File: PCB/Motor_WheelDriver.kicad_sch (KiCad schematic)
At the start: 21 parts, among them J7 39501-1002, J8 39501-1002, U1 125700D00000G, U2 125700D00000G

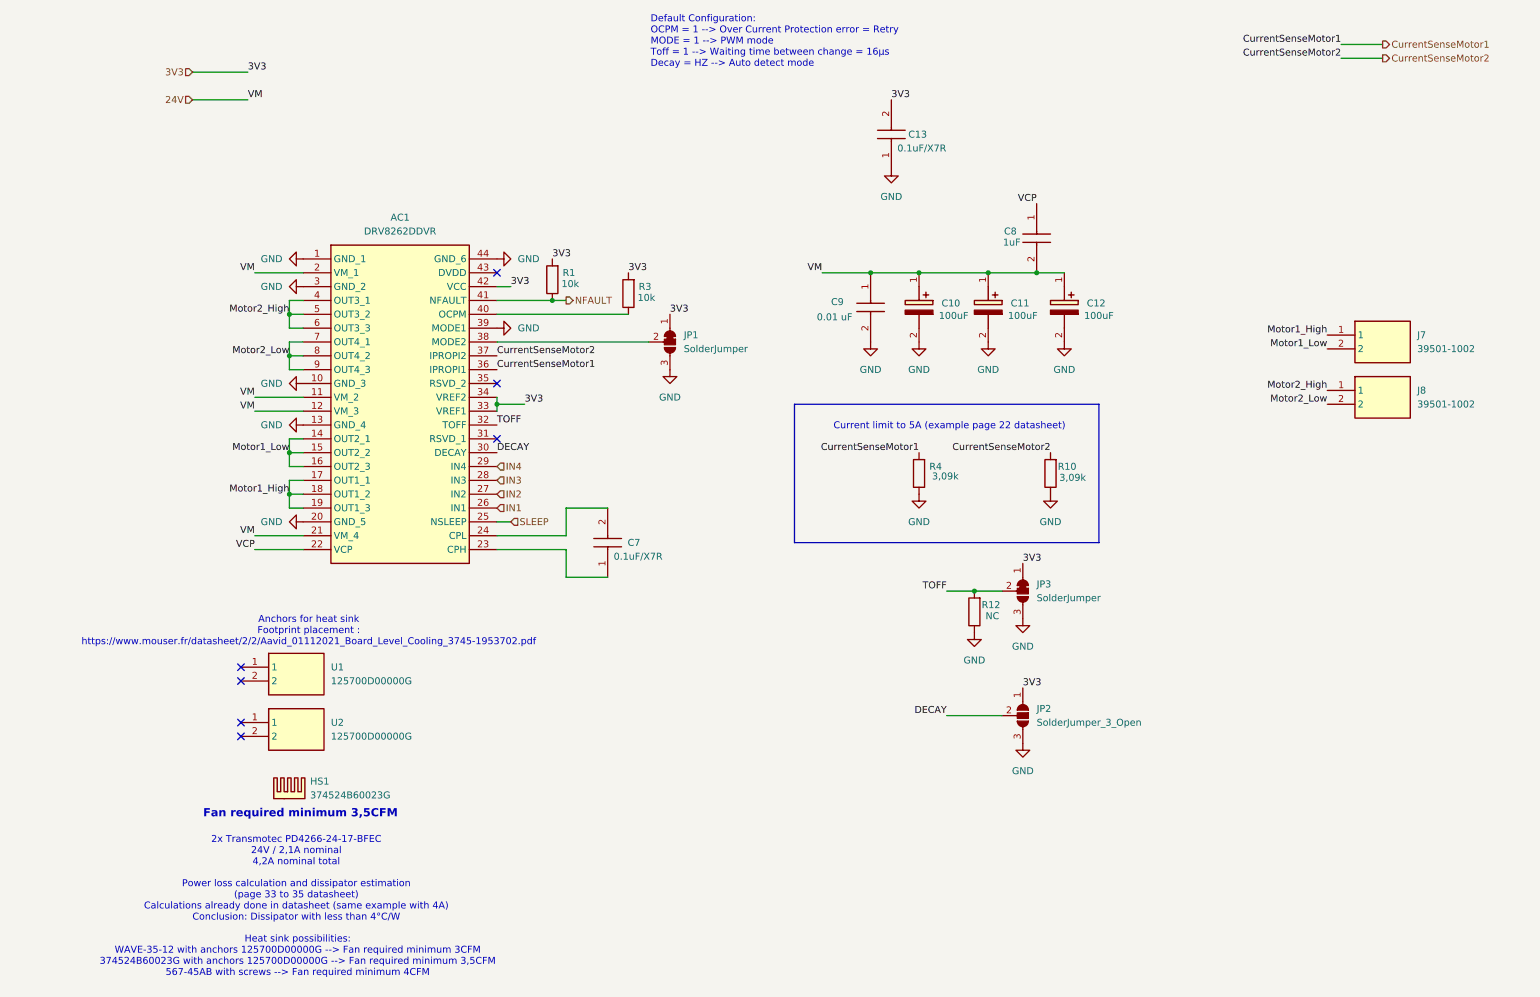
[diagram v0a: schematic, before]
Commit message: Updated a lot of stuff:
Added encoders,
Added 5V power supply for actuators
Added 12V power supply for actuators
Renamed sheets to be clearer
Added usb debug
Modify MCU sheet to be A3 format
Linked some pins
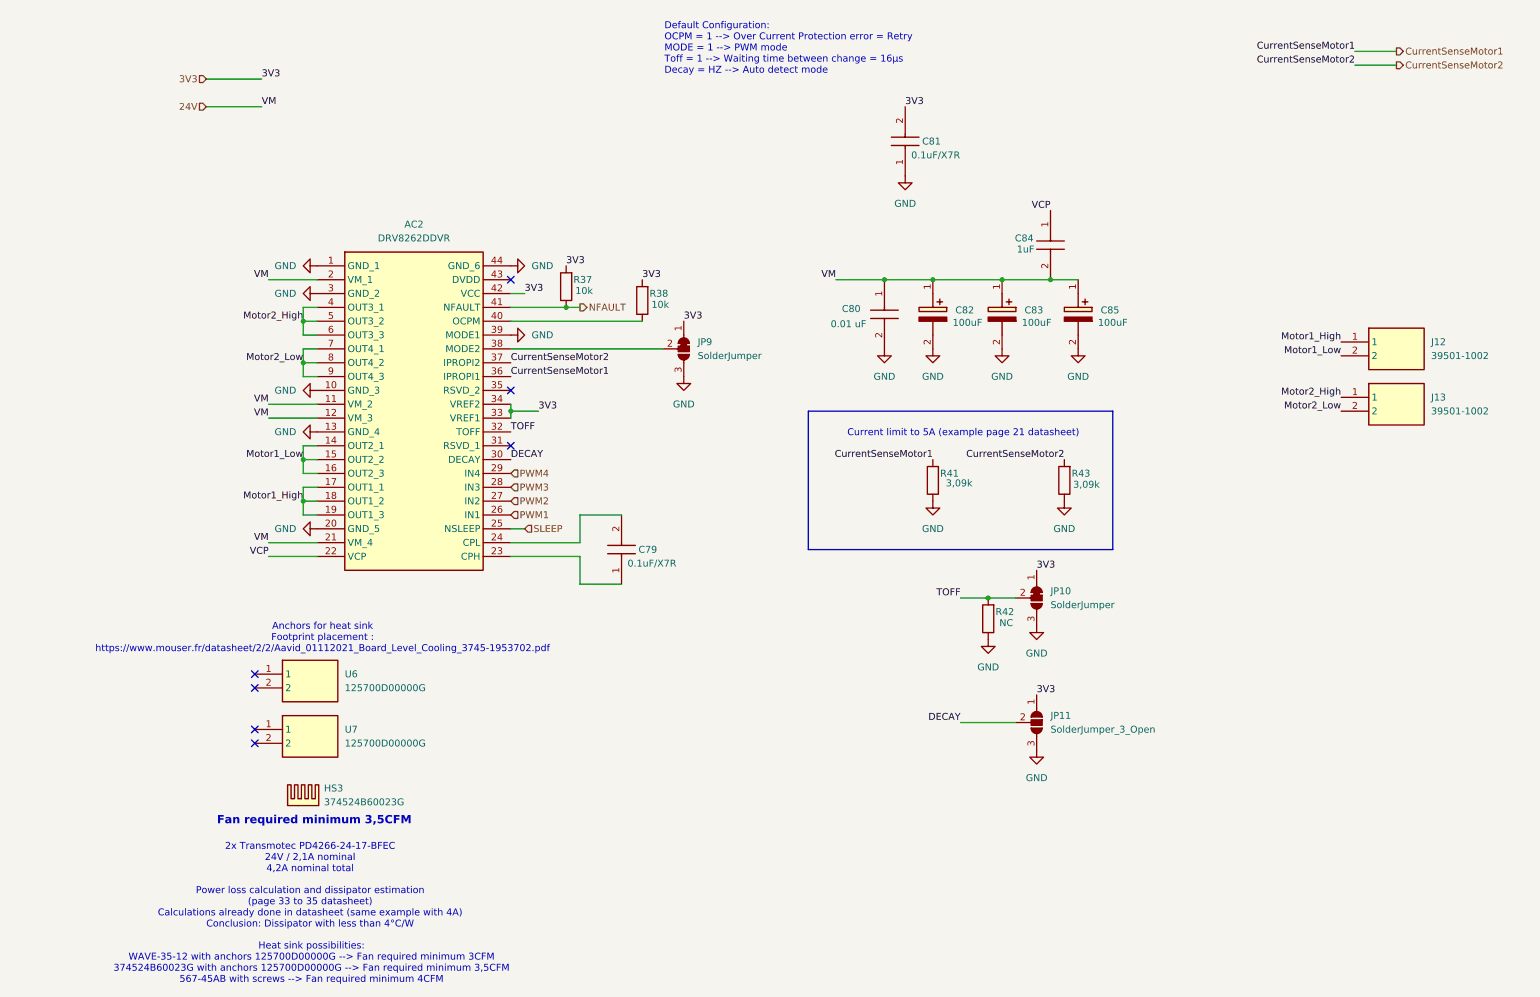
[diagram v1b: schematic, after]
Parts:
- removed AC1: DRV8262DDVR, SOP64P810X120-44N, symbol SamacSys:DRV8262DDVR
- removed C10, C11, C12: 100uF, CAPAE660X800N, symbol SamacSys_Parts:UCH1V101MCS1GS
- removed C13, C7: 0.1uF/X7R, CAPC2012X94N, symbol SamacSys_Parts:0805DC104MAT2A
- removed C8: 1uF, CAPC2012X94N, symbol SamacSys_Parts:0805DC104MAT2A
- removed C9: 0.01 uF, CAPC2012X94N, symbol SamacSys_Parts:0805DC104MAT2A
- removed HS1: 374524B60023G, symbol Mechanical:Heatsink
- removed J7, J8: 39501-1002, 395011002, symbol SamacSys:39501-1002
- removed JP1, JP3: SolderJumper, Jumper:SolderJumper-3_P1.3mm_Bridged12_RoundedPad1.0x1.5mm, symbol Jumper:SolderJumper_3_Bridged12
- removed JP2: SolderJumper_3_Open, symbol Jumper:SolderJumper_3_Open
- removed R1, R3: 10k, symbol Device:R
- removed R10, R4: 3,09k, symbol Device:R
- removed R12: NC, symbol Device:R
- removed U1, U2: 125700D00000G, 125700D00000G, symbol SamacSys_new:125700D00000G
- added AC2: DRV8262DDVR, SOP64P810X120-44N, symbol SamacSys:DRV8262DDVR
- added C79, C81: 0.1uF/X7R, CAPC2012X94N, symbol SamacSys_Parts:0805DC104MAT2A
- added C80: 0.01 uF, CAPC2012X94N, symbol SamacSys_Parts:0805DC104MAT2A
- added C82, C83, C85: 100uF, CAPAE660X800N, symbol SamacSys_Parts:UCH1V101MCS1GS
- added C84: 1uF, CAPC2012X94N, symbol SamacSys_Parts:0805DC104MAT2A
- added HS3: 374524B60023G, symbol Mechanical:Heatsink
- added J12, J13: 39501-1002, 395011002, symbol SamacSys:39501-1002
- added JP10, JP9: SolderJumper, Jumper:SolderJumper-3_P1.3mm_Bridged12_RoundedPad1.0x1.5mm, symbol Jumper:SolderJumper_3_Bridged12
- added JP11: SolderJumper_3_Open, symbol Jumper:SolderJumper_3_Open
- added R37, R38: 10k, symbol Device:R
- added R41, R43: 3,09k, symbol Device:R
- added R42: NC, symbol Device:R
- added U6, U7: 125700D00000G, 125700D00000G, symbol SamacSys_new:125700D00000G
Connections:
- net 24V: now also AC2.11 (VM_2), AC2.12 (VM_3), AC2.2 (VM_1), AC2.21 (VM_4), C80.1, C82.1 (+), C83.1 (+), C84.2, C85.1 (+)
- net 3V3: now also AC2.33 (VREF1), AC2.34 (VREF2), AC2.42 (VCC), C81.2, JP10.1 (A), JP11.1 (A), JP9.1 (A), R37.2, R38.2
- net CurrentSenseMotor1: now also AC2.36 (IPROPI1), R41.2
- net CurrentSenseMotor2: now also AC2.37 (IPROPI2), R43.2
- net DECAY: now also AC2.30 (DECAY), JP11.2 (C)
- net GND: now also AC2.1 (GND_1), AC2.10 (GND_3), AC2.13 (GND_4), AC2.20 (GND_5), AC2.3 (GND_2), AC2.39 (MODE1), AC2.44 (GND_6), C80.2, C81.1, C82.2 (-), C83.2 (-), C85.2 (-), JP10.3 (B), JP11.3 (B), JP9.3 (B), R41.1, R42.1, R43.1
- net Motor1_High: now also AC2.17 (OUT1_1), AC2.18 (OUT1_2), AC2.19 (OUT1_3), J12.1
- net Motor1_Low: now also AC2.14 (OUT2_1), AC2.15 (OUT2_2), AC2.16 (OUT2_3), J12.2
- net Motor2_High: now also AC2.4 (OUT3_1), AC2.5 (OUT3_2), AC2.6 (OUT3_3), J13.1
- net Motor2_Low: now also AC2.7 (OUT4_1), AC2.8 (OUT4_2), AC2.9 (OUT4_3), J13.2
- net NFAULT: now also AC2.41 (NFAULT), R37.1
- net SLEEP: now also AC2.25 (NSLEEP)
- net TOFF: now also AC2.32 (TOFF), JP10.2 (C), R42.2
- net VCP: now also AC2.22 (VCP), C84.1
- new net: AC2.23 (CPH), C79.1
- new net: AC2.24 (CPL), C79.2
- new net: AC2.38 (MODE2), JP9.2 (C)
- new net: AC2.40 (OCPM), R38.1
- new net PWM1: AC2.26 (IN1)
- new net PWM2: AC2.27 (IN2)
- new net PWM3: AC2.28 (IN3)
- new net PWM4: AC2.29 (IN4)
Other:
- note added: "Current limit to 5A (example page 21 datasheet)"
- note removed: "Current limit to 5A (example page 22 datasheet)"
